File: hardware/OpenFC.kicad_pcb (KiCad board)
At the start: 6 copper layers, 38.9 x 38.9 mm, 165 parts, among them J1 5V, J10 5V, J11 5V, J12 5V, J13 5V, J14 5V, J15 5V, J16 5V, J17 5V, J18 5V, J19 5V, J2 5V, J20 5V, J21 5V, J22 5V, J23 5V, J24 5V, J25 5V, J26 5V, J27 5V, J28 5V, J29 5V, J3 5V, J30 5V, J31 5V, J32 5V, J33 5V, J34 5V, J35 5V, J36 5V, J37 5V, J38 5V, J39 5V, J4 5V, J40 5V, J41 5V, J42 5V, J43 5V, J44 5V, J47 5V, J48 5V, J49 5V, J5 5V, J50 5V, J51 5V, J52 5V, J53 5V, J54 5V, J55 5V, J6 5V, J7 5V, J8 5V, J9 5V, P1 SM08B-SRSS-TB(LF)(SN), Q1 AP1606, Q2 AP1606, U1 TS2306A 240GF MSM 9_C2976675, U10 SN74LVC1G3157DTBR, U11 COS8051SOT, U12 TLV7031DPWR, U2 RP2354B_C39843328, U3 TI LMR51430YFDDCR, U4 TI LMR51430YFDDCR, U5 TPS2116DRLR, U6 NCV8187AMT180TAG, U7 LP5912-3.3DRVR, U8 SM06B-SRSS-TB(LF)(SN), U9 LSM6DSV16XTR, X1 XTM25012000JT00351001

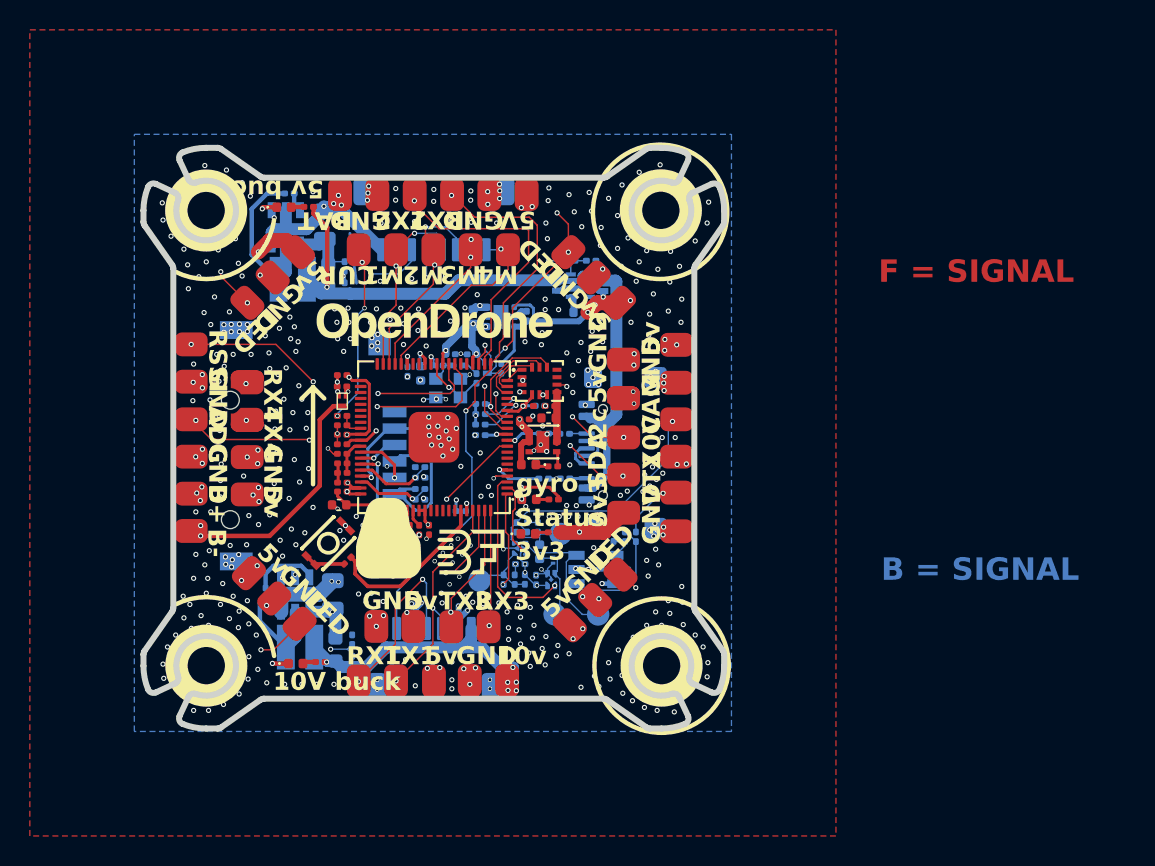
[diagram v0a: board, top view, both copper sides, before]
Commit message: Re-route with connectors
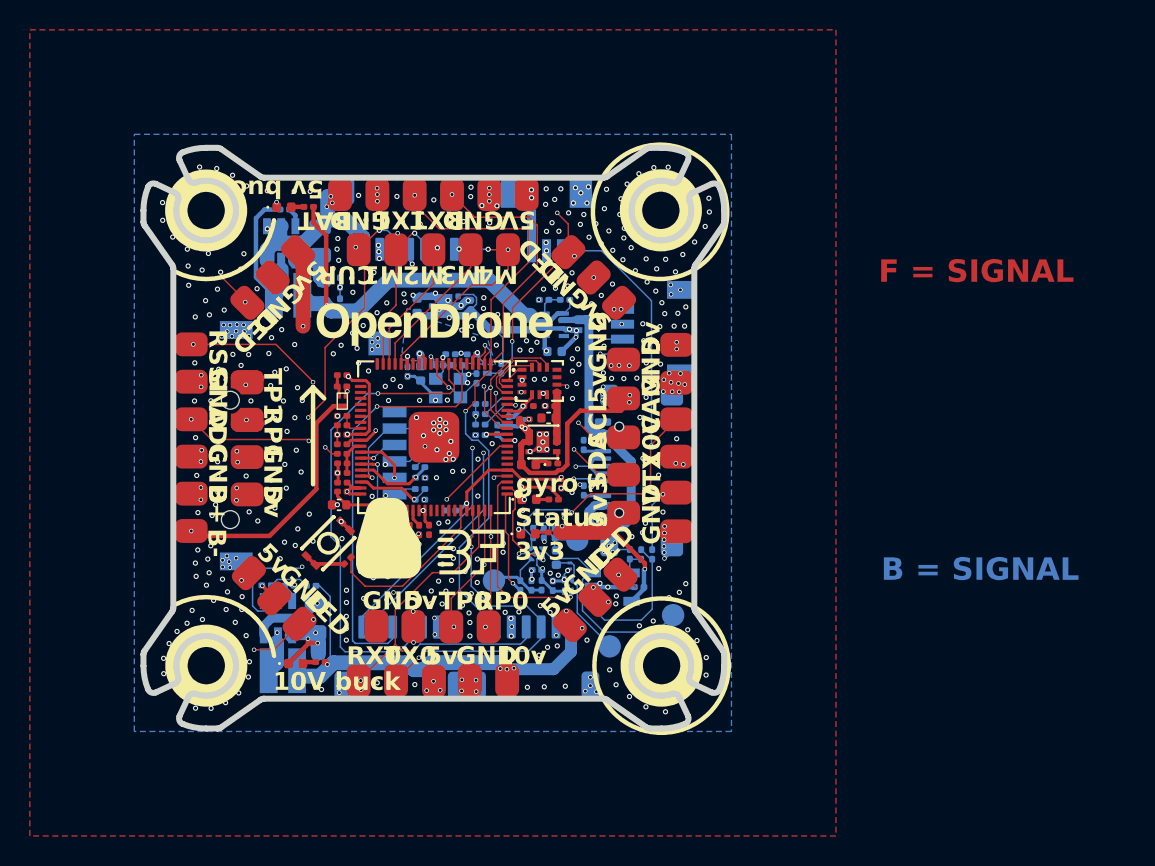
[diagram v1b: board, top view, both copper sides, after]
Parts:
- added CN1: SM04B-SRSS-TB, lib:CONN-SMD_4P-P1.00_SM04B-SRSS-TB-LF-SN, B.Cu at (167.7, 80.0)
- added U13: SM03B-SRSS-TB, lib:CONN-SMD_SM03B-SRSS-TB-LF-SN-P, B.Cu at (160.6, 72.7)
- added U14: SM06B-SRSS-TB(LF)(SN), lib:CONN-SMD_SM06B-SRSS-TB-LF-SN, B.Cu at (150.8, 101.8)
- C10: moved to F.Cu
- moved R22 6.79 mm to (141.9, 97.0), turned to 180 degrees
- moved U8 6.68 mm to (159.8, 101.7)
- moved R21 5.74 mm to (144.9, 97.0), turned to 0 degrees
- moved TP4 5.02 mm to (169.1, 99.0), turned to -135 degrees
- moved TP3 4.27 mm to (164.9, 101.1), turned to -135 degrees
- moved C30 3.83 mm to (155.6, 78.2)
- moved U7 3.83 mm to (153.8, 78.3)
- moved C32 3.83 mm to (152.0, 78.3)
- moved C28 3.15 mm to (161.2, 81.4)
- moved D3 3.15 mm to (162.7, 79.6)
- moved U5 3.15 mm to (161.2, 79.6)
- moved R19 3.15 mm to (161.9, 77.9)
- moved R20 3.15 mm to (160.5, 77.9)
- moved D2 3.15 mm to (159.6, 79.6)
- moved C1 3.13 mm to (157.3, 86.6), turned to 90 degrees
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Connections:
- net /PADS/PIOUART1_TX renamed /PADS/PU1TX
- USB1 pad A6: /RP2350A/D+_C -> /RP2350A/D+
- USB1 pad A7: /RP2350A/D-_C -> /RP2350A/D-
- USB1 pad B6: /RP2350A/D+_C -> /RP2350A/D+
- USB1 pad B7: /RP2350A/D-_C -> /RP2350A/D-
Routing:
- net GND: track 62.1 -> 101.4 mm, vias 447 -> 482
- net /PADS/PU1RX: track 28.6 -> 54.1 mm
- net /PADS/PIOUART0_TX: track 8.72 -> 29.6 mm, vias 1 -> 3
- net /PADS/I2C0.SCL: track 11.2 -> 31.4 mm
- net /PADS/PU1TX: track 19.4 -> 39.4 mm
- net /PADS/PIOUART0_RX: track 7.85 -> 27.6 mm, vias 2 -> 3
- net /PADS/I2C0.SDA: track 12.6 -> 31.9 mm
- net /OSD/VIDEO_IN: track 17.2 -> 35.0 mm, vias 1 -> 2
- net /RP2350A/D-: track 0.00 -> 17.5 mm, vias 1 -> 2
- net /RP2350A/D+: track 0.00 -> 16.6 mm, vias 1 -> 2
- net +10V: track 42.9 -> 54.8 mm, vias 8 -> 6
- net +3.3V: track 61.0 -> 51.4 mm, vias 22 -> 16
- net +5V: track 50.4 -> 59.3 mm, vias 26 -> 28
- net /PADS/UART0_TX: track 15.1 -> 22.9 mm
- net /PADS/UART0_RX: track 19.1 -> 26.4 mm
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- added copper zone on B.Cu, net +3.3V
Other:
- board text added: "Open"
- board text added: "RP0"
- board text added: "RP1"
- board text added: "RX0"
- board text added: "SBUS"
- board text added: "SCL"
- board text added: "TEL"
- board text added: "TP0"
- board text added: "TP1"
- board text added: "TX0"
- board text added: "gnd"
- board text added: "lite"
- board text removed: "+"
- board text removed: "-"
- board text removed: "1"
- board text removed: "10v buck"
- board text removed: "2"
- board text removed: "3"
- board text removed: "3v3 LDO"
- board text removed: "4"
- board text removed: "5v power switch"
- board text removed: "C"
- board text removed: "G"
- board text removed: "I2c"
- board text removed: "Lite"
- board text removed: "OPEN"
- board text removed: "OSD PIO"
- board text removed: "OSDLVL"
- board text removed: "R0"
- board text removed: "R1"
- board text removed: "RX2"
- board text removed: "RX3"
- board text removed: "RX4"
- board text removed: "SPDT"
- board text removed: "T"
- board text removed: "T0"
- board text removed: "TX2"
- board text removed: "TX3"
- board text removed: "TX4"
- board text removed: "VID_DC"
- board text removed: "crystal"
